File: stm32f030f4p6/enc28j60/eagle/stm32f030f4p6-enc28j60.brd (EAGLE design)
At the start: 68.6 x 53.4 mm, 33 parts, among them IC2 LM1117IDTX-3.3, IC3 LP2950, X1 MINI-USB-UX60-MB-5ST

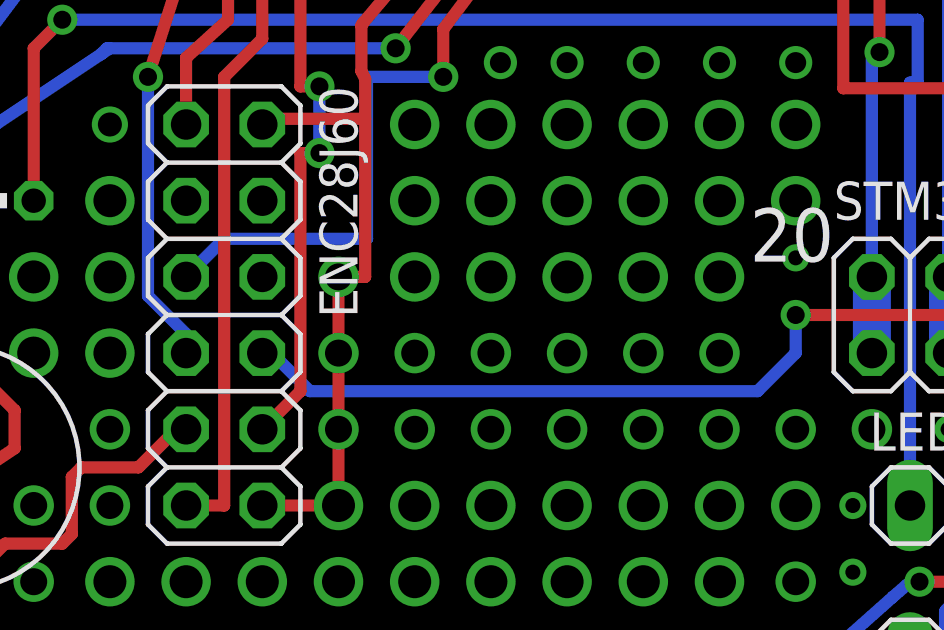
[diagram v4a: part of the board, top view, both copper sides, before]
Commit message: Fixed MISO-MOSI
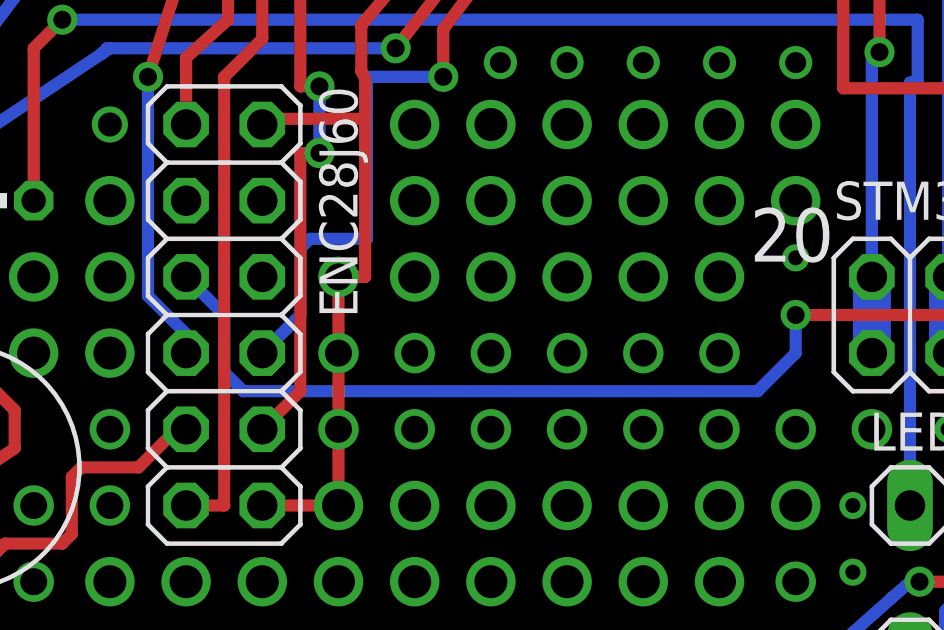
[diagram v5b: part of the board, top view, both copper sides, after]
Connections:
- net PA5 renamed PA5_SCK
- removed net PA6: ENC28J60.8, IC1.25, STM32F030F4PX_R.17, STM32F030F4PX_R.18
- removed net PA7: ENC28J60.5, IC1.24, STM32F030F4PX_R.15, STM32F030F4PX_R.16
- new net PA6_MISO: ENC28J60.5, IC1.25, STM32F030F4PX_R.17, STM32F030F4PX_R.18
- new net PA7_MOSI: ENC28J60.8, IC1.24, STM32F030F4PX_R.15, STM32F030F4PX_R.16
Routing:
- net PA7: track 111.8 -> 0.00 mm, vias 3 -> 0
- net PA7_MOSI: track 0.00 -> 111.7 mm, vias 0 -> 3
- net PA6_MISO: track 0.00 -> 99.8 mm, vias 0 -> 2
- net PA6: track 95.1 -> 0.00 mm, vias 2 -> 0
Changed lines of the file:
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@@
 <wire x1="67.945" y1="13.97" x2="66.675" y2="15.24" width="0.4064" layer="16"/>
 </signal>
-<signal name="PA5">
+<signal name="PA5_SCK">
 <contactref element="STM32F030F4PX_R" pad="19"/>
 <contactref element="STM32F030F4PX_R" pad="20"/>
@@
 <wire x1="28.956" y1="46.99" x2="28.956" y2="50.8" width="0.4064" layer="1"/>
 </signal>
-<signal name="PA6">
+<signal name="PA6_MISO">
 <contactref element="STM32F030F4PX_R" pad="18"/>
 <contactref element="STM32F030F4PX_R" pad="17"/>
@@
 <wire x1="63.5" y1="44.45" x2="63.5" y2="38.1" width="0.4064" layer="16"/>
 <wire x1="63.5" y1="38.1" x2="60.96" y2="35.56" width="0.4064" layer="16"/>
-<contactref element="ENC28J60" pad="8"/>
-<wire x1="20.32" y1="33.02" x2="20.6375" y2="33.02" width="0.4064" layer="16"/>
-<wire x1="20.6375" y1="33.02" x2="21.9075" y2="31.75" width="0.4064" layer="16"/>
-<wire x1="21.9075" y1="31.75" x2="36.83" y2="31.75" width="0.4064" layer="16"/>
+<wire x1="19.685" y1="31.75" x2="36.83" y2="31.75" width="0.4064" layer="16"/>
 <wire x1="36.83" y1="31.75" x2="38.1" y2="33.02" width="0.4064" layer="16"/>
 <wire x1="38.1" y1="33.02" x2="38.1" y2="34.29" width="0.4064" layer="16"/>
@@
 <wire x1="38.1" y1="34.29" x2="59.69" y2="34.29" width="0.4064" layer="1"/>
 <wire x1="59.69" y1="34.29" x2="60.96" y2="35.56" width="0.4064" layer="1"/>
+<contactref element="ENC28J60" pad="5"/>
+<wire x1="19.685" y1="31.75" x2="19.05" y2="32.385" width="0.4064" layer="16"/>
+<wire x1="19.05" y1="32.385" x2="19.05" y2="34.29" width="0.4064" layer="16"/>
+<wire x1="19.05" y1="34.29" x2="17.78" y2="35.56" width="0.4064" layer="16"/>
 </signal>
 <signal name="N$15">
@@
 <wire x1="20.955" y1="46.99" x2="20.955" y2="49.2125" width="0.4064" layer="1"/>
 </signal>
-<signal name="PA7">
-<contactref element="ENC28J60" pad="5"/>
+<signal name="PA7_MOSI">
 <contactref element="IC1" pad="24"/>
 <contactref element="STM32F030F4PX_R" pad="16"/>
@@
 <wire x1="58.42" y1="48.5775" x2="34.036" y2="48.5775" width="0.4064" layer="16"/>
 <wire x1="34.036" y1="48.5775" x2="34.036" y2="50.8" width="0.4064" layer="16"/>
-<wire x1="17.78" y1="35.56" x2="19.05" y2="36.83" width="0.4064" layer="16"/>
-<wire x1="19.05" y1="36.83" x2="23.8125" y2="36.83" width="0.4064" layer="16"/>
 <wire x1="23.8125" y1="36.83" x2="23.8125" y2="42.2275" width="0.4064" layer="16"/>
 <wire x1="39.6875" y1="41.8465" x2="44.45" y2="41.8465" width="0.4064" layer="1"/>
@@
 <wire x1="26.3525" y1="42.2275" x2="23.8125" y2="42.2275" width="0.4064" layer="16"/>
 <wire x1="62.5475" y1="38.4175" x2="62.5475" y2="42.2275" width="0.4064" layer="16"/>
+<contactref element="ENC28J60" pad="8"/>
+<wire x1="23.8125" y1="36.83" x2="21.9075" y2="36.83" width="0.4064" layer="16"/>
+<wire x1="21.9075" y1="36.83" x2="21.59" y2="36.5125" width="0.4064" layer="16"/>
+<wire x1="21.59" y1="36.5125" x2="21.59" y2="34.29" width="0.4064" layer="16"/>
+<wire x1="21.59" y1="34.29" x2="20.32" y2="33.02" width="0.4064" layer="16"/>
 </signal>
 <signal name="GND_RAW">
